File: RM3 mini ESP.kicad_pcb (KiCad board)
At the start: 2 copper layers, 46.3 x 43 mm, 21 parts, among them J1 USB_C_Receptacle_USB2.0, J2 Conn_01x06_Male, J3 Conn_01x06_Male, J4 Conn_01x03_Male, U1 ESP-12F, U2 AMS1117-3.3

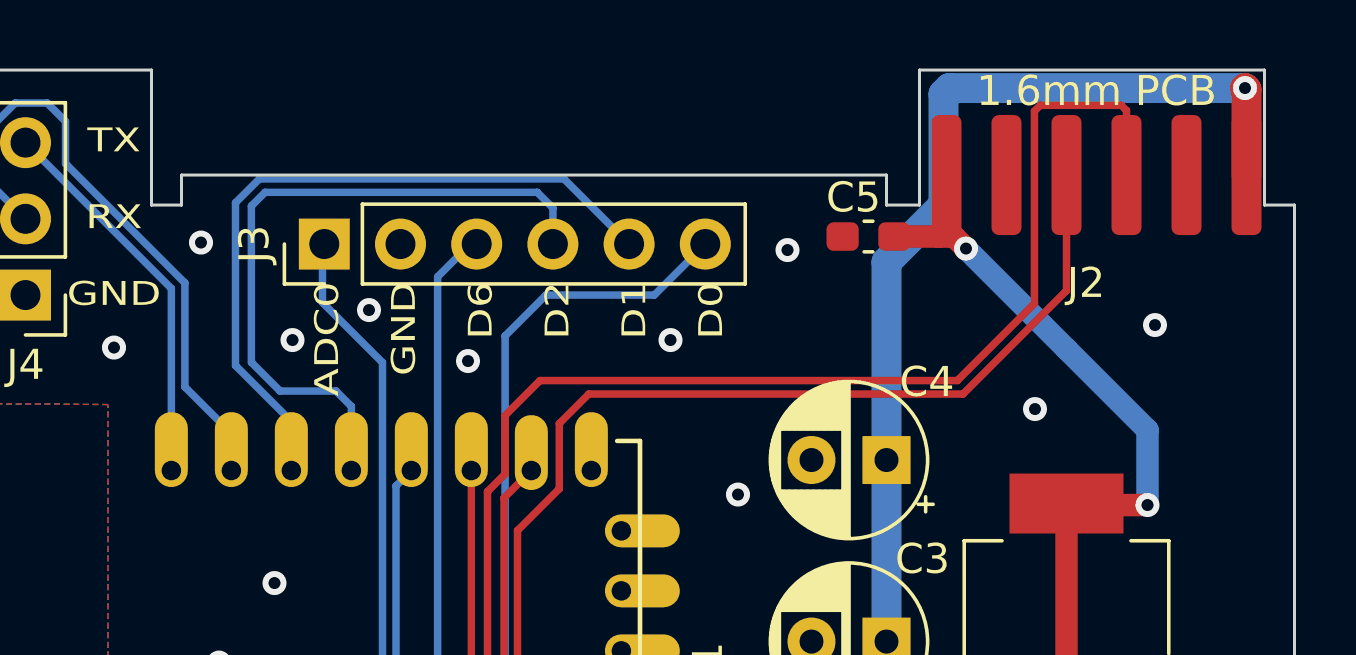
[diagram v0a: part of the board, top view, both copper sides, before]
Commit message: Small correction for edge connector
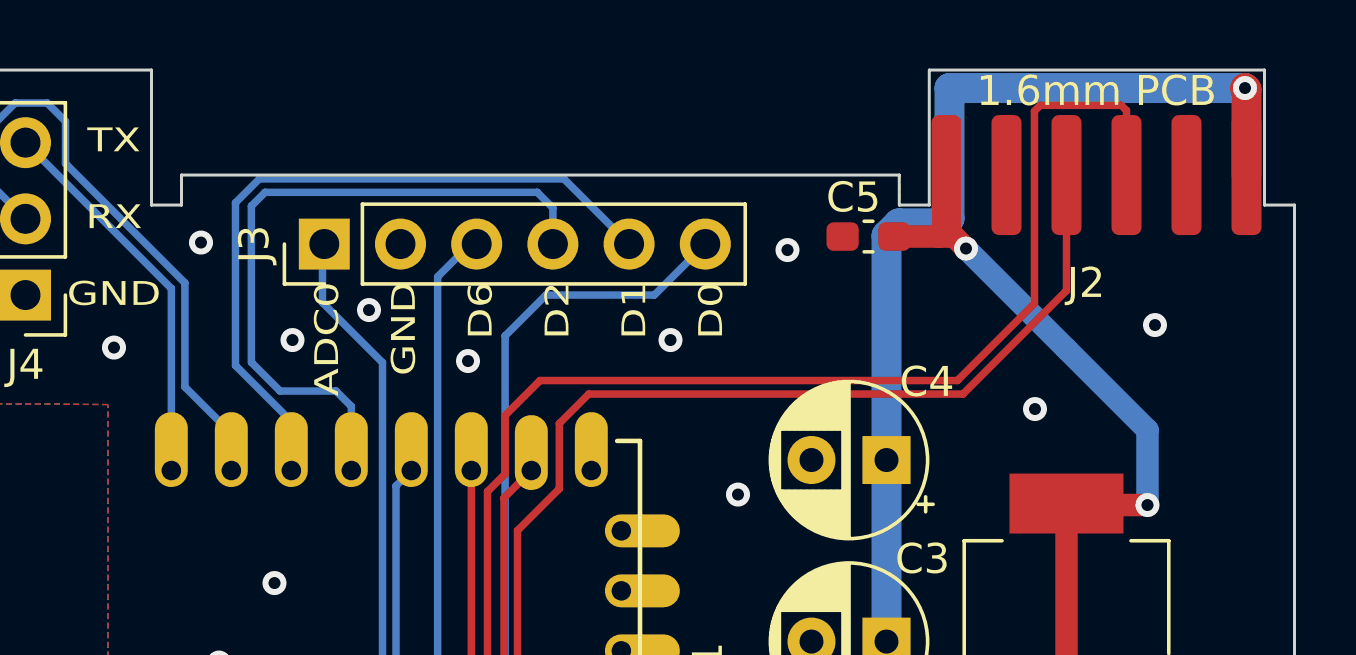
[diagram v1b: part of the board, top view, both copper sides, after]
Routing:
- net /5V: track 59.7 -> 60.6 mm
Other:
- outline, holes or cut-outs redrawn
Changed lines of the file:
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@@
   (gr_line (start 49.7 110) (end 55.7 110) (layer "Edge.Cuts") (width 0.1))
   (gr_line (start 48.4 108) (end 49.7 108) (layer "Edge.Cuts") (width 0.1))
-  (gr_line (start 77.6 67) (end 77.6 71.5) (layer "Edge.Cuts") (width 0.1))
+  (gr_line (start 77.9272 67) (end 77.9272 71.5) (layer "Edge.Cuts") (width 0.1))
   (gr_line (start 57.1 110) (end 90.1 110) (layer "Edge.Cuts") (width 0.1))
   (gr_line (start 53 70.5) (end 53 71.5) (layer "Edge.Cuts") (width 0.1))
   (gr_line (start 49.7 108) (end 49.7 110) (layer "Edge.Cuts") (width 0.1))
-  (gr_line (start 77.6 71.5) (end 76.5 71.5) (layer "Edge.Cuts") (width 0.1))
-  (gr_line (start 89.1 67) (end 77.6 67) (layer "Edge.Cuts") (width 0.1))
+  (gr_line (start 77.9272 71.5) (end 76.9272 71.5) (layer "Edge.Cuts") (width 0.1))
+  (gr_line (start 89.1 67) (end 77.9272 67) (layer "Edge.Cuts") (width 0.1))
   (gr_line (start 48.4 110) (end 48.4 108) (layer "Edge.Cuts") (width 0.1))
-  (gr_line (start 76.5 71.5) (end 76.5 70.5) (layer "Edge.Cuts") (width 0.1))
+  (gr_line (start 76.9272 71.5) (end 76.9272 70.5) (layer "Edge.Cuts") (width 0.1))
   (gr_line (start 57.1 108) (end 57.1 110) (layer "Edge.Cuts") (width 0.1))
   (gr_line (start 52 67) (end 43.8 67) (layer "Edge.Cuts") (width 0.1))
@@
   (gr_line (start 53 71.5) (end 52 71.5) (layer "Edge.Cuts") (width 0.1))
   (gr_line (start 90.1 110) (end 90.1 71.5) (layer "Edge.Cuts") (width 0.1))
-  (gr_line (start 76.5 70.5) (end 53 70.5) (layer "Edge.Cuts") (width 0.1))
+  (gr_line (start 76.9272 70.5) (end 53 70.5) (layer "Edge.Cuts") (width 0.1))
   (gr_line (start 89.1 71.5) (end 89.1 67) (layer "Edge.Cuts") (width 0.1))
   (gr_line (start 55.7 110) (end 55.7 108) (layer "Edge.Cuts") (width 0.1))
@@
   (via (at 80.2 94.35) (size 0.8) (drill 0.4) (layers "F.Cu" "B.Cu") (net 7))
   (via (at 88.45 67.6) (size 0.8) (drill 0.4) (layers "F.Cu" "B.Cu") (net 7))
-  (segment (start 76.5 73.4) (end 76.5 80) (width 1) (layer "B.Cu") (net 7))
+  (segment (start 78.6 67.6) (end 78.6 71.944365) (width 1) (layer "B.Cu") (net 7))
+  (segment (start 76.5 72.5218) (end 76.5 80) (width 1) (layer "B.Cu") (net 7))
+  (segment (start 78.433765 72.1106) (end 76.9112 72.1106) (width 1) (layer "B.Cu") (net 7))
   (segment (start 88.45 67.6) (end 78.6 67.6) (width 1) (layer "B.Cu") (net 7))
-  (segment (start 78.4 67.8) (end 78.4 71.5) (width 1) (layer "B.Cu") (net 7))
-  (segment (start 78.6 67.6) (end 78.4 67.8) (width 1) (layer "B.Cu") (net 7))
   (segment (start 76.5 80) (end 76.5 86.05) (width 1) (layer "B.Cu") (net 7))
   (segment (start 76.5 86.05) (end 76.5 90.65) (width 1) (layer "B.Cu") (net 7))
-  (segment (start 78.4 71.5) (end 76.5 73.4) (width 1) (layer "B.Cu") (net 7))
   (segment (start 76.5 90.65) (end 80.2 94.35) (width 1) (layer "B.Cu") (net 7))
+  (segment (start 76.9112 72.1106) (end 76.5 72.5218) (width 1) (layer "B.Cu") (net 7))
+  (segment (start 78.6 71.944365) (end 78.433765 72.1106) (width 1) (layer "B.Cu") (net 7))
   (segment (start 88.8 106.1125) (end 88.8 101.303274) (width 0.25) (layer "F.Cu") (net 8))
   (segment (start 85.446726 97.95) (end 81.955 97.95) (width 0.25) (layer "F.Cu") (net 8))
@@
         (xy 53 71.5)
         (xy 53 70.5)
-        (xy 76.5 70.5)
-        (xy 76.5 71.5)
-        (xy 77.6 71.5)
-        (xy 77.6 67)
+        (xy 76.9366 70.485)
+        (xy 76.9366 71.5)
+        (xy 77.9272 71.5)
+        (xy 77.9272 67)
         (xy 89.1 67)
         (xy 89.1 71.5)

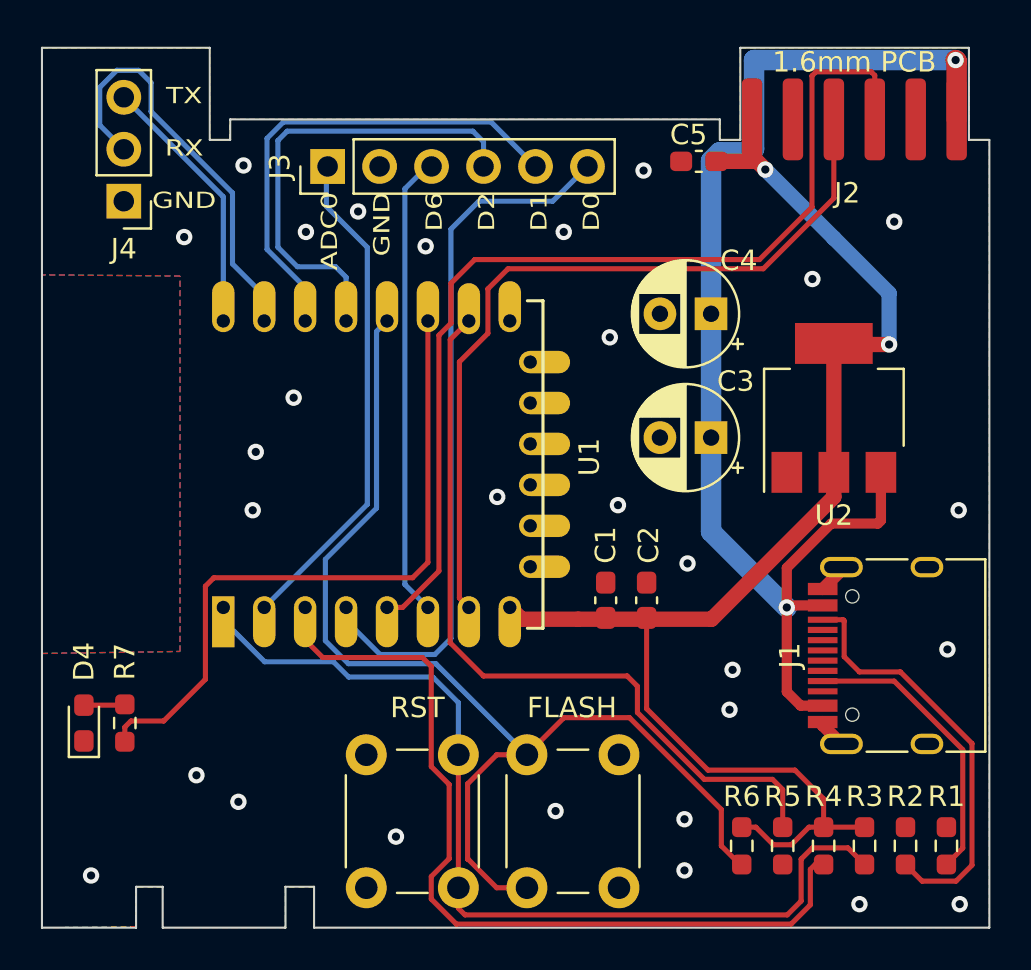
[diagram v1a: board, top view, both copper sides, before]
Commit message: minimal size adjust to fit the case
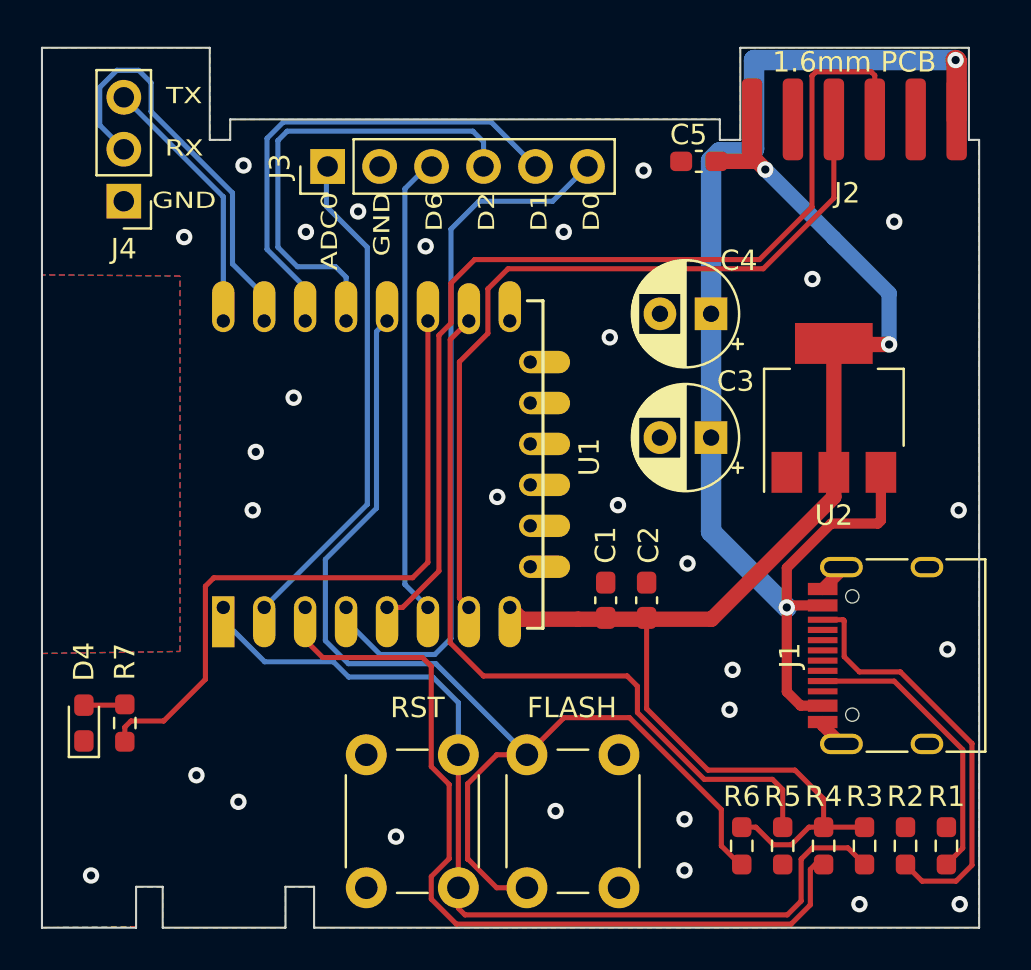
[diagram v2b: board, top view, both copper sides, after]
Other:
- board size 46.3 x 43 mm -> 45.8 x 43 mm
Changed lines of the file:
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@@
   (gr_line (start 48.4 108) (end 49.7 108) (layer "Edge.Cuts") (width 0.1))
   (gr_line (start 77.9272 67) (end 77.9272 71.5) (layer "Edge.Cuts") (width 0.1))
-  (gr_line (start 57.1 110) (end 90.1 110) (layer "Edge.Cuts") (width 0.1))
+  (gr_line (start 57.1 110) (end 89.6 110) (layer "Edge.Cuts") (width 0.1))
   (gr_line (start 53 70.5) (end 53 71.5) (layer "Edge.Cuts") (width 0.1))
   (gr_line (start 49.7 108) (end 49.7 110) (layer "Edge.Cuts") (width 0.1))
@@
   (gr_line (start 43.8 110) (end 48.4 110) (layer "Edge.Cuts") (width 0.1))
   (gr_line (start 53 71.5) (end 52 71.5) (layer "Edge.Cuts") (width 0.1))
-  (gr_line (start 90.1 110) (end 90.1 71.5) (layer "Edge.Cuts") (width 0.1))
+  (gr_line (start 89.6 110) (end 89.6 71.5) (layer "Edge.Cuts") (width 0.1))
   (gr_line (start 76.9272 70.5) (end 53 70.5) (layer "Edge.Cuts") (width 0.1))
   (gr_line (start 89.1 71.5) (end 89.1 67) (layer "Edge.Cuts") (width 0.1))
   (gr_line (start 55.7 110) (end 55.7 108) (layer "Edge.Cuts") (width 0.1))
-  (gr_line (start 90.1 71.5) (end 89.1 71.5) (layer "Edge.Cuts") (width 0.1))
+  (gr_line (start 89.6 71.5) (end 89.1 71.5) (layer "Edge.Cuts") (width 0.1))
   (gr_line (start 43.8 67) (end 43.8 110) (layer "Edge.Cuts") (width 0.1))
   (gr_line (start 52 71.5) (end 52 67) (layer "Edge.Cuts") (width 0.1))
@@
         (xy 89.1 67)
         (xy 89.1 71.5)
-        (xy 90.1 71.5)
-        (xy 90.1 110)
+        (xy 89.6112 71.501)
+        (xy 89.5858 110)
         (xy 57.1 110)
         (xy 57.1 108)
